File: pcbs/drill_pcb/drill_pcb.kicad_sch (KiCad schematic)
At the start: 28 parts, among them J1 WEIGHT SENSOR, J10 DC MOTOR UART, J11 motor1, J12 motor2, J2 DC MOTOR 24 V, J3 LIMIT SENSOR TOP, J4 LIMIT SENSOR BOTTOM, J5 ENCODER VERTICAL DRIVE, J6 ENCODER STORAGE, J7 HEIGHT SENSOR, J8 STEPPER VERTICAL DRIVE, J9 STEPPER STORAGE, U1 LM3940, U101 TXS0108EPW, U102 ESP32-DevKitC

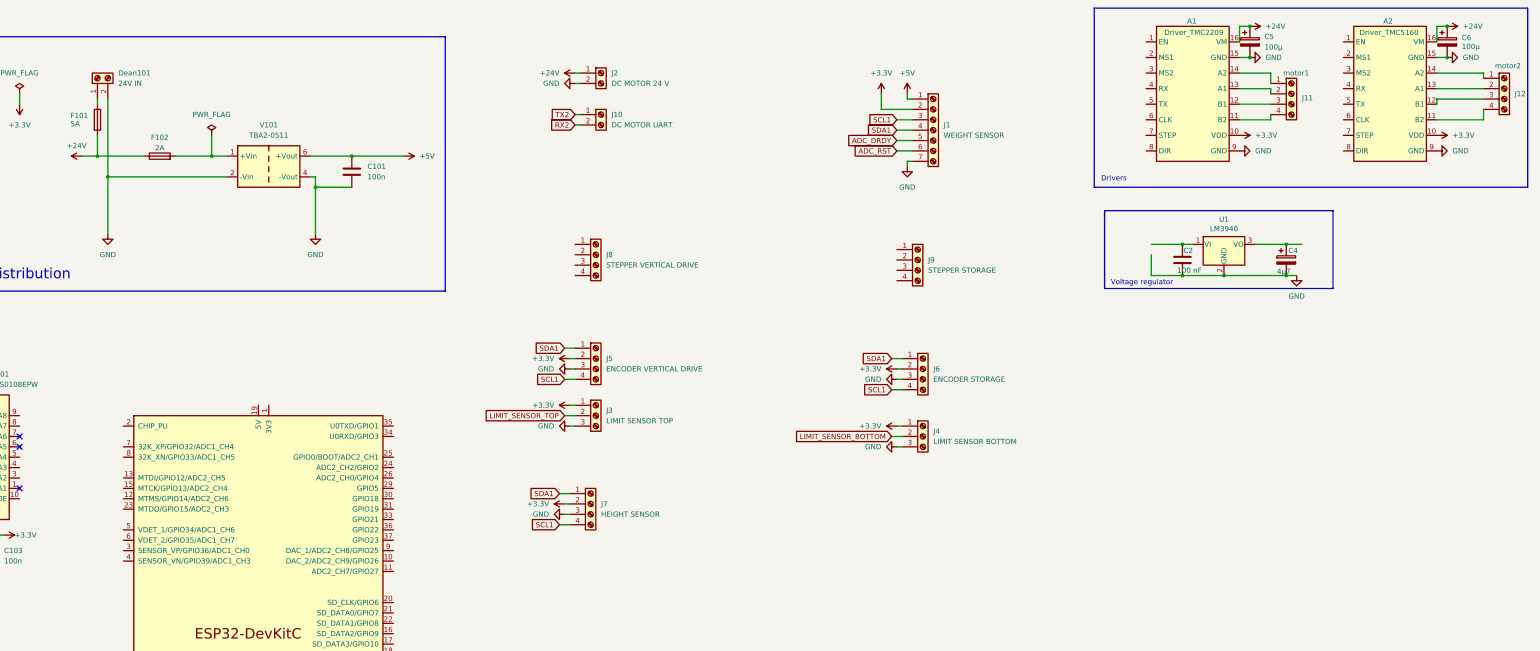
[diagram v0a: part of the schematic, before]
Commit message: driver pin update
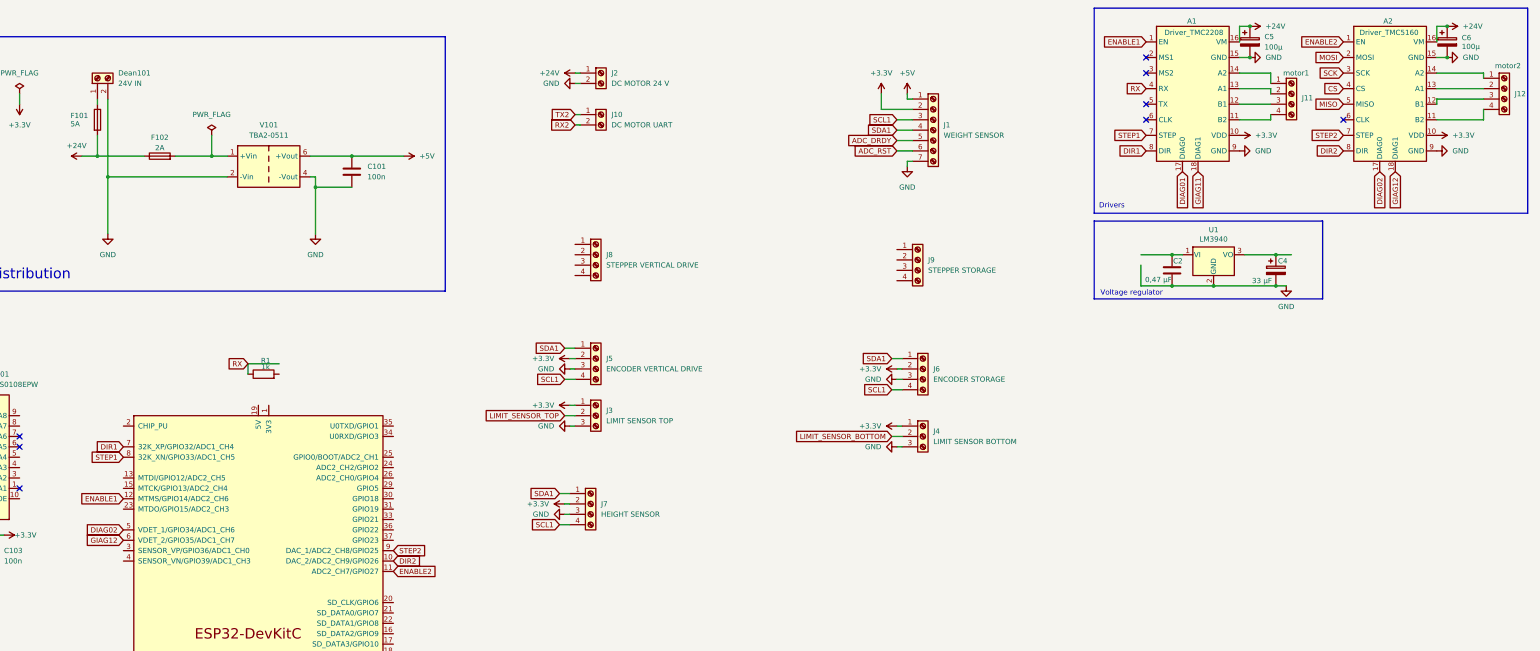
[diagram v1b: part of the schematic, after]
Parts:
- added R1: 1k, Resistor_SMD:R_1206_3216Metric, symbol Device:R
- A1: value Driver_TMC2209 -> Driver_TMC2208; footprint Module:Pololu_Breakout-16_15.2x20.3mm -> ds
- A2: footprint Module:Pololu_Breakout-16_15.2x20.3mm -> sd
- C2: value 100 nF -> 0,47 μF
- C4: value 4μ7 -> 33 μF
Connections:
- net ENABLE2: now reaches A2.1 (EN)
- net ENABLE2: now also U102.11 (ADC2_CH7/GPIO27)
- net MOSI: now reaches A2.2 (MOSI)
- net SCK: now reaches A2.3 (SCK)
- net CS: now reaches A2.4 (CS)
- net MISO: now reaches A2.5 (MISO)
- net STEP2: now reaches A2.7 (STEP)
- net STEP2: now also U102.9 (DAC_1/ADC2_CH8/GPIO25)
- net DIR2: now reaches A2.8 (DIR)
- net DIR2: now also U102.10 (DAC_2/ADC2_CH9/GPIO26)
- net ENABLE1: now reaches A1.1 (EN)
- net ENABLE1: now also U102.12 (MTMS/GPIO14/ADC2_CH6)
- net RX: now reaches A1.4 (RX)
- net RX: now also R1.1
- net STEP1: now reaches A1.7 (STEP)
- net STEP1: now also U102.8 (32K_XN/GPIO33/ADC1_CH5)
- net DIR1: now reaches A1.8 (DIR)
- net DIR1: now also U102.7 (32K_XP/GPIO32/ADC1_CH4)
- net DIAG02: now reaches U102.5 (VDET_1/GPIO34/ADC1_CH6)
- net DIAG02: now also A2.17 (DIAG0)
- net GIAG12: now reaches U102.6 (VDET_2/GPIO35/ADC1_CH7)
- net GIAG12: now also A2.18 (DIAG1)
- new net DIAG01: A1.17 (DIAG0)
- new net GIAG11: A1.18 (DIAG1)
- no-connect marks 6 -> 11
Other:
- moved on the sheet: C2, C4, U1

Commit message: Further work on the PCB. Schematic complete AFAIK. Routing in progress.
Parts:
- removed C102, C103: 100n, Capacitor_SMD:C_1206_3216Metric_Pad1.33x1.80mm_HandSolder, symbol Device:C
- removed C2: 0,47 μF, Capacitor_THT:C_Disc_D4.3mm_W1.9mm_P5.00mm, symbol Device:C
- removed J10: DC MOTOR UART, drill_T-DEAN:DEANS, symbol Connector:Screw_Terminal_01x02
- removed J8: STEPPER VERTICAL DRIVE, Connector_JST:JST_XH_B4B-XH-A_1x04_P2.50mm_Vertical, symbol Connector:Screw_Terminal_01x04
- removed J9: STEPPER STORAGE, Connector_JST:JST_XH_B4B-XH-A_1x04_P2.50mm_Vertical, symbol Connector:Screw_Terminal_01x04
- removed U101: TXS0108EPW, Package_SO:TSSOP-20_4.4x6.5mm_P0.65mm, symbol Logic_LevelTranslator:TXS0108EPW
- added C1: 33 μF, Capacitor_THT:CP_Radial_D5.0mm_P2.50mm, symbol Device:C_Polarized
- added C4: 100n, Capacitor_SMD:C_1206_3216Metric_Pad1.33x1.80mm_HandSolder, symbol Device:C
- added J3: DC MOTOR UART, Connector_JST:JST_XH_B3B-XH-A_1x03_P2.50mm_Vertical, symbol Connector:Screw_Terminal_01x03
- J11: value motor1 -> STEPPER STORAGE
- J7: renamed from J12; value motor2 -> STEPPER VERTICAL DRIVE
- renumbered A2 to A1, A1 to A2, C101 to C2, C4 to C3, C6 to C5, C5 to C6, F101 to F1, F102 to F2, Dean101 to J1, J1 to J10, J5 to J4, J3 to J5, J7 to J6, J6 to J8, J4 to J9, U102 to U1, U1 to U2, V101 to V1
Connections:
- net CS is gone; now on net VSPI_CS1: A1.4 (CS)
- net DIAG01 is gone; now on net DRVR_STORAGE_0: A2.17 (DIAG0)
- net GIAG11 is gone; now on net DRVR_STORAGE_1: A2.18 (DIAG1)
- net MISO is gone; now on net VSPI_MISO: A1.5 (MISO)
- net MOSI is gone; now on net VSPI_MOSI: A1.2 (MOSI)
- net RX is gone; now on net RX1: A2.4 (RX), R1.1
- net SCK is gone; now on net VSPI_SCK: A1.3 (SCK)
- net +3.3V: now also C3.1, U1.1 (3V3), U2.3 (VO), C4.1
- net +5V: now also U2.1 (VI), C1.1
- net ADC_DRDY: now also U1.26 (ADC2_CH0/GPIO4)
- net ADC_RST: now also U1.24 (ADC2_CH2/GPIO2)
- net GND: now also C1.2, C4.2, J3.1 (Pin_1)
- net LIMIT_SENSOR_BOTTOM: now also U1.23 (MTDO/GPIO15/ADC2_CH3)
- net LIMIT_SENSOR_TOP: now also U1.25 (GPIO0/BOOT/ADC2_CH1)
- net RX2: now also U1.27 (GPIO16), J3.3 (Pin_3)
- net SCL1: now also U1.36 (GPIO22)
- net SDA1: now also U1.33 (GPIO21)
- net TX2: now also U1.28 (GPIO17), J3.2 (Pin_2)
- net at R1.2: now also U1.8 (32K_XN/GPIO33/ADC1_CH5)
- net DRVR_STORAGE_DIR: now reaches U1.13 (MTDI/GPIO12/ADC2_CH5)
- net DRVR_STORAGE_DIR: now also A2.8 (DIR)
- net DRVR_STORAGE_STEP: now reaches U1.15 (MTCK/GPIO13/ADC2_CH4)
- net DRVR_STORAGE_STEP: now also A2.7 (STEP)
- net VSPI_CS1: now reaches U1.29 (GPIO5)
- net DRVR_STORAGE_0: now reaches U1.3 (SENSOR_VP/GPIO36/ADC1_CH0)
- net VSPI_SCK: now reaches U1.30 (GPIO18)
- net VSPI_MISO: now reaches U1.31 (GPIO19)
- net VSPI_MOSI: now reaches U1.37 (GPIO23)
- net DRVR_STORAGE_1: now reaches U1.4 (SENSOR_VN/GPIO39/ADC1_CH3)
- net DIAG02 renamed DRVR_VERT_DIAG0
- net DIR1 renamed RX1
- net RX1: no longer A2.8 (DIR)
- net DIR2 renamed DRVR_VERT_DIR
- net ENABLE1 renamed DRVR_STORAGE_ENABLE
- net ENABLE2 renamed DRVR_VERT_ENABLE
- net GIAG12 renamed DRVR_VERT_DIAG1
- removed net STEP1: A2.7 (STEP), U1.8 (32K_XN/GPIO33/ADC1_CH5)
- net STEP2 renamed DRVR_VERT_STEP
- no-connect marks 11 -> 15
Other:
- note removed: "Drivers"
- note removed: "Voltage regulator"
- moved on the sheet: A1, A2, C2, C3, C5, C6, F1, F2, J1, J10, J11, J2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

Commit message: PCB should be fully complete now. Somebody pls review it :(
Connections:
- net +24V: no longer F2.1
- net DRVR_STORAGE_0: now also U1.6 (VDET_2/GPIO35/ADC1_CH7); no longer U1.3 (SENSOR_VP/GPIO36/ADC1_CH0)
- net DRVR_STORAGE_1: now also U1.5 (VDET_1/GPIO34/ADC1_CH6); no longer U1.4 (SENSOR_VN/GPIO39/ADC1_CH3)
- net DRVR_STORAGE_DIR: now also U1.9 (DAC_1/ADC2_CH8/GPIO25); no longer U1.13 (MTDI/GPIO12/ADC2_CH5)
- net DRVR_STORAGE_ENABLE: now also U1.11 (ADC2_CH7/GPIO27); no longer U1.12 (MTMS/GPIO14/ADC2_CH6)
- net DRVR_STORAGE_STEP: now also U1.10 (DAC_2/ADC2_CH9/GPIO26); no longer U1.15 (MTCK/GPIO13/ADC2_CH4)
- net DRVR_VERT_DIAG0: now also U1.4 (SENSOR_VN/GPIO39/ADC1_CH3); no longer U1.5 (VDET_1/GPIO34/ADC1_CH6)
- net DRVR_VERT_DIAG1: now also U1.3 (SENSOR_VP/GPIO36/ADC1_CH0); no longer U1.6 (VDET_2/GPIO35/ADC1_CH7)
- net DRVR_VERT_DIR: now also U1.13 (MTDI/GPIO12/ADC2_CH5); no longer U1.10 (DAC_2/ADC2_CH9/GPIO26)
- net DRVR_VERT_ENABLE: now also U1.12 (MTMS/GPIO14/ADC2_CH6); no longer U1.11 (ADC2_CH7/GPIO27)
- net DRVR_VERT_STEP: now also U1.15 (MTCK/GPIO13/ADC2_CH4); no longer U1.9 (DAC_1/ADC2_CH8/GPIO25)
- net LIMIT_SENSOR_BOTTOM: now also U1.25 (GPIO0/BOOT/ADC2_CH1); no longer U1.23 (MTDO/GPIO15/ADC2_CH3)
- net LIMIT_SENSOR_TOP: now also U1.23 (MTDO/GPIO15/ADC2_CH3); no longer U1.25 (GPIO0/BOOT/ADC2_CH1)
- net at F1.1, J1.1 (Pin_1): now also F2.1
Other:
- moved on the sheet: C1, C2, C3, C4, F1, F2, U2, V1

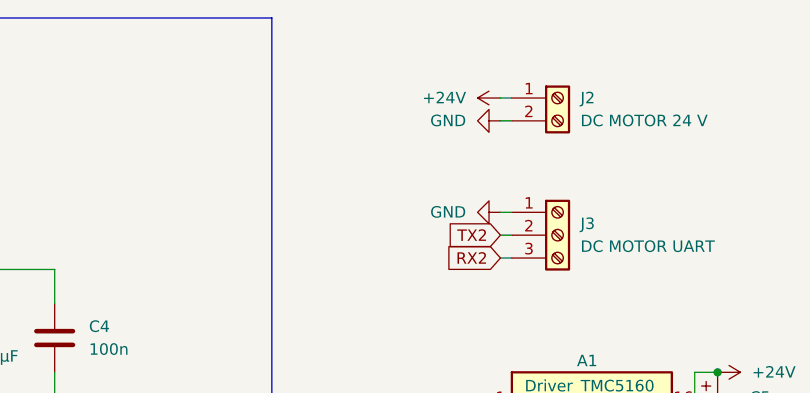
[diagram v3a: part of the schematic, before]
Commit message: Change capacitor sizes and re-export manufacturing files
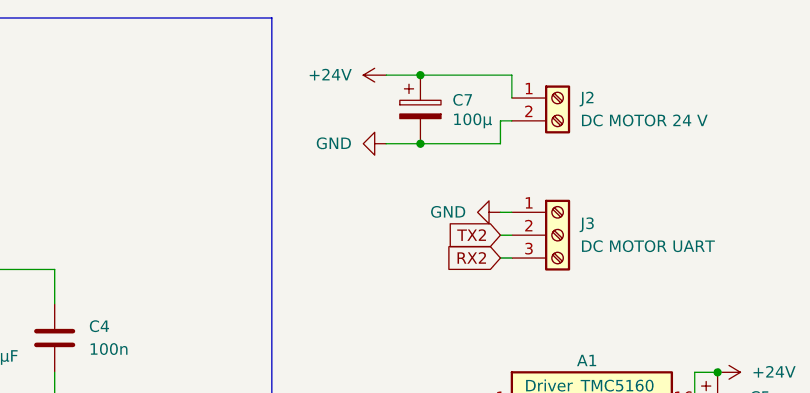
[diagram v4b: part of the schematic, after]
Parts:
- added C7: 100μ, Capacitor_THT:CP_Radial_D12.5mm_P5.00mm, symbol Device:C_Polarized
- C1, C3: footprint Capacitor_THT:CP_Radial_D5.0mm_P2.50mm -> Capacitor_THT:CP_Radial_D8.0mm_P3.50mm
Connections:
- net +24V: now also C7.1
- net GND: now also C7.2
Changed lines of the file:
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@@
 	)
 	(junction
+		(at 177.8 21.59)
+		(diameter 0)
+		(color 0 0 0 0)
+	)
+	(junction
+		(at 177.8 29.21)
+		(diameter 0)
+		(color 0 0 0 0)
+	)
+	(junction
 		(at 124.46 58.42)
 		(diameter 0)
@@
 	(wire
 		(pts
+			(xy 177.8 29.21) (xy 186.69 29.21)
+		)
+		(stroke
+			(width 0)
+			(type default)
+		)
+	)
+	(wire
+		(pts
 			(xy 53.34 48.26) (xy 55.88 48.26)
 		)
@@
 	(wire
 		(pts
+			(xy 173.99 21.59) (xy 177.8 21.59)
+		)
+		(stroke
+			(width 0)
+			(type default)
+		)
+	)
+	(wire
+		(pts
 			(xy 318.77 25.4) (xy 320.04 25.4)
 		)
@@
 	(wire
 		(pts
+			(xy 186.69 29.21) (xy 186.69 26.67)
+		)
+		(stroke
+			(width 0)
+			(type default)
+		)
+	)
+	(wire
+		(pts
 			(xy 96.52 54.61) (xy 96.52 58.42)
 		)
@@
 	(wire
 		(pts
+			(xy 186.69 26.67) (xy 187.96 26.67)
+		)
+		(stroke
+			(width 0)
+			(type default)
+		)
+	)
+	(wire
+		(pts
 			(xy 316.23 35.56) (xy 320.04 35.56)
 		)
@@
 	(wire
 		(pts
-			(xy 186.69 24.13) (xy 187.96 24.13)
+			(xy 53.34 58.42) (xy 53.34 48.26)
 		)
 		(stroke
@@
 	(wire
 		(pts
-			(xy 53.34 58.42) (xy 53.34 48.26)
+			(xy 63.5 118.11) (xy 64.77 118.11)
 		)
 		(stroke
@@
 	(wire
 		(pts
-			(xy 63.5 118.11) (xy 64.77 118.11)
+			(xy 77.47 58.42) (xy 83.82 58.42)
 		)
 		(stroke
@@
 	(wire
 		(pts
-			(xy 77.47 58.42) (xy 83.82 58.42)
+			(xy 187.96 21.59) (xy 187.96 24.13)
 		)
 		(stroke
@@
 	(wire
 		(pts
-			(xy 121.92 43.18) (xy 124.46 43.18)
+			(xy 177.8 21.59) (xy 187.96 21.59)
 		)
 		(stroke
@@
 	(wire
 		(pts
-			(xy 208.28 77.47) (xy 219.71 77.47)
+			(xy 173.99 29.21) (xy 177.8 29.21)
 		)
 		(stroke
@@
 	(wire
 		(pts
-			(xy 334.01 77.47) (xy 341.63 77.47)
+			(xy 121.92 43.18) (xy 124.46 43.18)
 		)
 		(stroke
@@
 	(wire
 		(pts
-			(xy 186.69 26.67) (xy 187.96 26.67)
+			(xy 208.28 77.47) (xy 219.71 77.47)
+		)
+		(stroke
+			(width 0)
+			(type default)
+		)
+	)
+	(wire
+		(pts
+			(xy 334.01 77.47) (xy 341.63 77.47)
 		)
 		(stroke
@@
 	)
 	(symbol
+		(lib_id "Device:C_Polarized")
+		(at 177.8 25.4 0)
+		(unit 1)
+		(exclude_from_sim no)
+		(in_bom yes)
+		(on_board yes)
+		(dnp no)
+		(property "Reference" "C7"
+			(at 181.356 24.384 0)
+			(effects
+				(font
+					(size 1.27 1.27)
+				)
+				(justify left)
+			)
+		)
+		(property "Value" "100μ"
+			(at 181.356 26.5429 0)
+			(effects
+				(font
+					(size 1.27 1.27)
+				)
+				(justify left)
+			)
+		)
+		(property "Footprint" "Capacitor_THT:CP_Radial_D12.5mm_P5.00mm"
+			(at 178.7652 29.21 0)
+			(effects
+				(font
+					(size 1.27 1.27)
+				)
+				(hide yes)
+			)
+		)
+		(property "Datasheet" "~"
+			(at 177.8 25.4 0)
+			(effects
+				(font
+					(size 1.27 1.27)
+				)
+				(hide yes)
+			)
+		)
+		(property "Description" "Polarized capacitor"
+			(at 177.8 25.4 0)
+			(effects
+				(font
+					(size 1.27 1.27)
+				)
+				(hide yes)
+			)
+		)
+		(pin "2"
+		)
+		(pin "1"
+		)
+		(instances
+			(project "drill_pcb"
+				(path "/bebf97b1-2f7f-4d03-a427-fe976f4b2313"
+					(reference "C7")
+					(unit 1)
+				)
+			)
+		)
+	)
+	(symbol
 		(lib_id "power:+3.3V")
 		(at 318.77 27.94 90)
@@
 	(symbol
 		(lib_id "power:GND")
-		(at 186.69 26.67 270)
+		(at 173.99 29.21 270)
 		(unit 1)
 		(exclude_from_sim no)
@@
 		(fields_autoplaced yes)
 		(property "Reference" "#PWR08"
-			(at 180.34 26.67 0)
+			(at 167.64 29.21 0)
 			(effects
 				(font
@@
 		)
 		(property "Value" "GND"
-			(at 182.88 26.6699 90)
+			(at 170.18 29.2099 90)
 			(effects
 				(font
@@
 		)
 		(property "Footprint" ""
-			(at 186.69 26.67 0)
+			(at 173.99 29.21 0)
 			(effects
 				(font
@@
 		)
 		(property "Datasheet" ""
-			(at 186.69 26.67 0)
+			(at 173.99 29.21 0)
 			(effects
 				(font
@@
 		)
 		(property "Description" "Power symbol creates a global label with name \"GND\" , ground"
-			(at 186.69 26.67 0)
+			(at 173.99 29.21 0)
 			(effects
 				(font
@@
 			)
 		)
-		(property "Footprint" "Capacitor_THT:CP_Radial_D5.0mm_P2.50mm"
+		(property "Footprint" "Capacitor_THT:CP_Radial_D8.0mm_P3.50mm"
 			(at 84.7852 54.61 0)
 			(effects
@@
 			)
 		)
-		(property "Footprint" "Capacitor_THT:CP_Radial_D5.0mm_P2.50mm"
+		(property "Footprint" "Capacitor_THT:CP_Radial_D8.0mm_P3.50mm"
 			(at 125.4252 54.61 0)
 			(effects
@@
 	(symbol
 		(lib_id "power:+24V")
-		(at 186.69 24.13 90)
+		(at 173.99 21.59 90)
 		(unit 1)
 		(exclude_from_sim no)
@@
 		(fields_autoplaced yes)
 		(property "Reference" "#PWR07"
-			(at 190.5 24.13 0)
+			(at 177.8 21.59 0)
 			(effects
 				(font
@@
 		)
 		(property "Value" "+24V"
-			(at 182.88 24.1299 90)
+			(at 170.18 21.5899 90)
 			(effects
 				(font
@@
 		)
 		(property "Footprint" ""
-			(at 186.69 24.13 0)
+			(at 173.99 21.59 0)
 			(effects
 				(font
@@
 		)
 		(property "Datasheet" ""
-			(at 186.69 24.13 0)
+			(at 173.99 21.59 0)
 			(effects
 				(font
@@
 		)
 		(property "Description" "Power symbol creates a global label with name \"+24V\""
-			(at 186.69 24.13 0)
+			(at 173.99 21.59 0)
 			(effects
 				(font

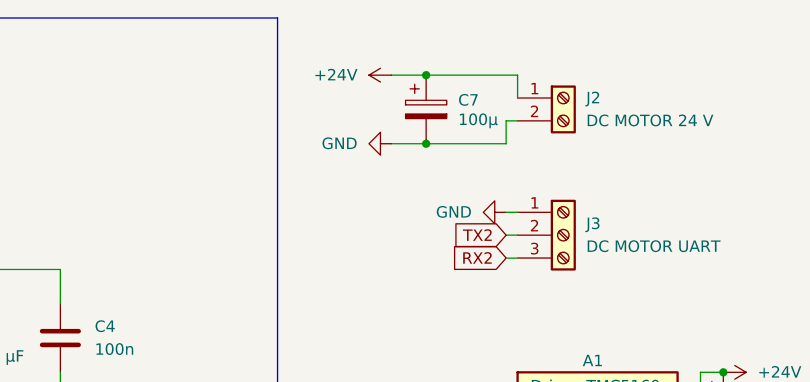
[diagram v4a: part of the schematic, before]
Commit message: added fuse library
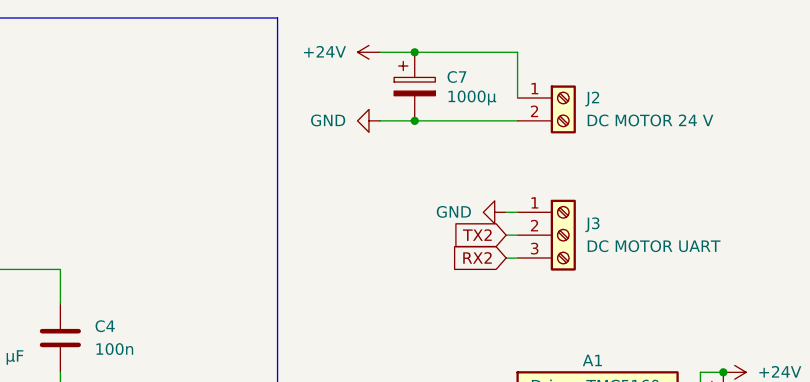
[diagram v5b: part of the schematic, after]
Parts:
- C7: value 100μ -> 1000μ
- F1, F2: footprint Fuse:Fuse_Blade_ATO_directSolder -> drill_fuseSlot:fuseSlot
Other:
- moved on the sheet: C7
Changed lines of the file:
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@@
 	)
 	(junction
-		(at 177.8 21.59)
+		(at 176.53 19.05)
 		(diameter 0)
 		(color 0 0 0 0)
 	)
 	(junction
-		(at 177.8 29.21)
+		(at 176.53 26.67)
 		(diameter 0)
 		(color 0 0 0 0)
@@
 	(wire
 		(pts
-			(xy 177.8 29.21) (xy 186.69 29.21)
+			(xy 176.53 26.67) (xy 187.96 26.67)
 		)
 		(stroke
@@
 	(wire
 		(pts
-			(xy 173.99 21.59) (xy 177.8 21.59)
+			(xy 172.72 19.05) (xy 176.53 19.05)
 		)
 		(stroke
@@
 	(wire
 		(pts
-			(xy 186.69 29.21) (xy 186.69 26.67)
-		)
-		(stroke
-			(width 0)
-			(type default)
-		)
-	)
-	(wire
-		(pts
 			(xy 96.52 54.61) (xy 96.52 58.42)
 		)
@@
 	(wire
 		(pts
-			(xy 186.69 26.67) (xy 187.96 26.67)
-		)
-		(stroke
-			(width 0)
-			(type default)
-		)
-	)
-	(wire
-		(pts
 			(xy 316.23 35.56) (xy 320.04 35.56)
 		)
@@
 	(wire
 		(pts
-			(xy 187.96 21.59) (xy 187.96 24.13)
+			(xy 187.96 19.05) (xy 187.96 24.13)
 		)
 		(stroke
@@
 	(wire
 		(pts
-			(xy 177.8 21.59) (xy 187.96 21.59)
+			(xy 176.53 19.05) (xy 187.96 19.05)
 		)
 		(stroke
@@
 	(wire
 		(pts
-			(xy 173.99 29.21) (xy 177.8 29.21)
+			(xy 172.72 26.67) (xy 176.53 26.67)
 		)
 		(stroke
@@
 			)
 		)
-		(property "Footprint" "Fuse:Fuse_Blade_ATO_directSolder"
+		(property "Footprint" "drill_fuseSlot:fuseSlot"
 			(at 36.83 34.798 90)
 			(effects
@@
 	(symbol
 		(lib_id "Device:C_Polarized")
-		(at 177.8 25.4 0)
+		(at 176.53 22.86 0)
 		(unit 1)
 		(exclude_from_sim no)
@@
 		(dnp no)
 		(property "Reference" "C7"
-			(at 181.356 24.384 0)
+			(at 180.086 21.844 0)
 			(effects
 				(font
@@
 			)
 		)
-		(property "Value" "100μ"
-			(at 181.356 26.5429 0)
+		(property "Value" "1000μ"
+			(at 180.086 24.0029 0)
 			(effects
 				(font
@@
 		)
 		(property "Footprint" "Capacitor_THT:CP_Radial_D12.5mm_P5.00mm"
-			(at 178.7652 29.21 0)
+			(at 177.4952 26.67 0)
 			(effects
 				(font
@@
 		)
 		(property "Datasheet" "~"
-			(at 177.8 25.4 0)
+			(at 176.53 22.86 0)
 			(effects
 				(font
@@
 		)
 		(property "Description" "Polarized capacitor"
-			(at 177.8 25.4 0)
+			(at 176.53 22.86 0)
 			(effects
 				(font
@@
 	(symbol
 		(lib_id "power:GND")
-		(at 173.99 29.21 270)
+		(at 172.72 26.67 270)
 		(unit 1)
 		(exclude_from_sim no)
@@
 		(fields_autoplaced yes)
 		(property "Reference" "#PWR08"
-			(at 167.64 29.21 0)
+			(at 166.37 26.67 0)
 			(effects
 				(font
@@
 		)
 		(property "Value" "GND"
-			(at 170.18 29.2099 90)
+			(at 168.91 26.6699 90)
 			(effects
 				(font
@@
 		)
 		(property "Footprint" ""
-			(at 173.99 29.21 0)
+			(at 172.72 26.67 0)
 			(effects
 				(font
@@
 		)
 		(property "Datasheet" ""
-			(at 173.99 29.21 0)
+			(at 172.72 26.67 0)
 			(effects
 				(font
@@
 		)
 		(property "Description" "Power symbol creates a global label with name \"GND\" , ground"
-			(at 173.99 29.21 0)
+			(at 172.72 26.67 0)
 			(effects
 				(font
@@
 			)
 		)
-		(property "Footprint" "Fuse:Fuse_Blade_ATO_directSolder"
+		(property "Footprint" "drill_fuseSlot:fuseSlot"
 			(at 36.83 44.958 90)
 			(effects
@@
 	(symbol
 		(lib_id "power:+24V")
-		(at 173.99 21.59 90)
+		(at 172.72 19.05 90)
 		(unit 1)
 		(exclude_from_sim no)
@@
 		(fields_autoplaced yes)
 		(property "Reference" "#PWR07"
-			(at 177.8 21.59 0)
+			(at 176.53 19.05 0)
 			(effects
 				(font
@@
 		)
 		(property "Value" "+24V"
-			(at 170.18 21.5899 90)
+			(at 168.91 19.0499 90)
 			(effects
 				(font
@@
 		)
 		(property "Footprint" ""
-			(at 173.99 21.59 0)
+			(at 172.72 19.05 0)
 			(effects
 				(font
@@
 		)
 		(property "Datasheet" ""
-			(at 173.99 21.59 0)
+			(at 172.72 19.05 0)
 			(effects
 				(font
@@
 		)
 		(property "Description" "Power symbol creates a global label with name \"+24V\""
-			(at 173.99 21.59 0)
+			(at 172.72 19.05 0)
 			(effects
 				(font

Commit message: finished new fuse holder library. PCB tweaks.
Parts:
- F1, F2: footprint drill_fuseSlot:fuseSlot -> drill_fuseHolderATO:fuseHolderATO
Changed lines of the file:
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@@
 			)
 		)
-		(property "Footprint" "drill_fuseSlot:fuseSlot"
+		(property "Footprint" "drill_fuseHolderATO:fuseHolderATO"
 			(at 36.83 34.798 90)
 			(effects
@@
 			)
 		)
-		(property "Footprint" "drill_fuseSlot:fuseSlot"
+		(property "Footprint" "drill_fuseHolderATO:fuseHolderATO"
 			(at 36.83 44.958 90)
 			(effects
